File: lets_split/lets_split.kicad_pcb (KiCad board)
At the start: 2 copper layers, 112 x 79 mm, 62 parts, among them J1 3PIN, J2 6PIN, J3 3PIN, SW1 SW_PUSH, SW10 SW_PUSH, SW11 SW_PUSH, SW12 SW_PUSH, SW13 SW_PUSH, SW14 SW_PUSH, SW15 SW_PUSH, SW16 SW_PUSH, SW17 SW_PUSH, SW18 SW_PUSH, SW19 SW_PUSH, SW2 SW_PUSH, SW21 SW_PUSH, SW22 SW_PUSH, SW23 SW_PUSH, SW3 SW_PUSH, SW4 SW_PUSH, SW5 SW_PUSH, SW6 SW_PUSH, SW7 SW_PUSH, SW8 SW_PUSH, SW9 SW_PUSH, U2 HOLE, U3 HOLE, U4 HOLE, U5 HOLE

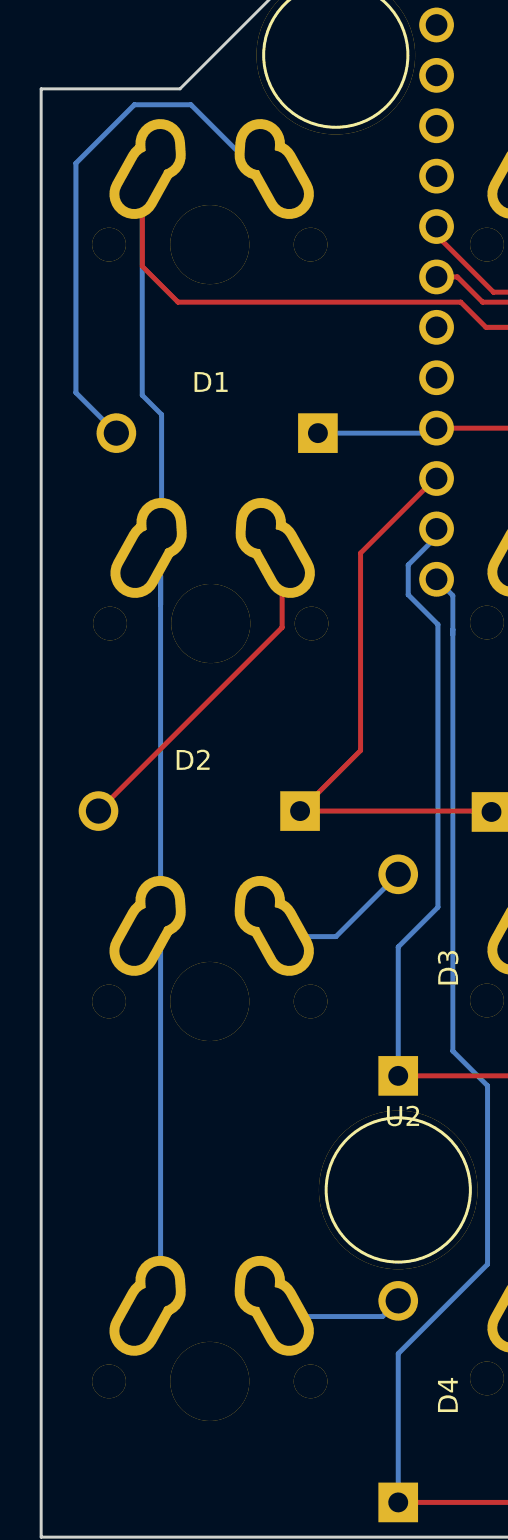
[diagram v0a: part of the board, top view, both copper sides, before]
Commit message: Fix alignments at left column
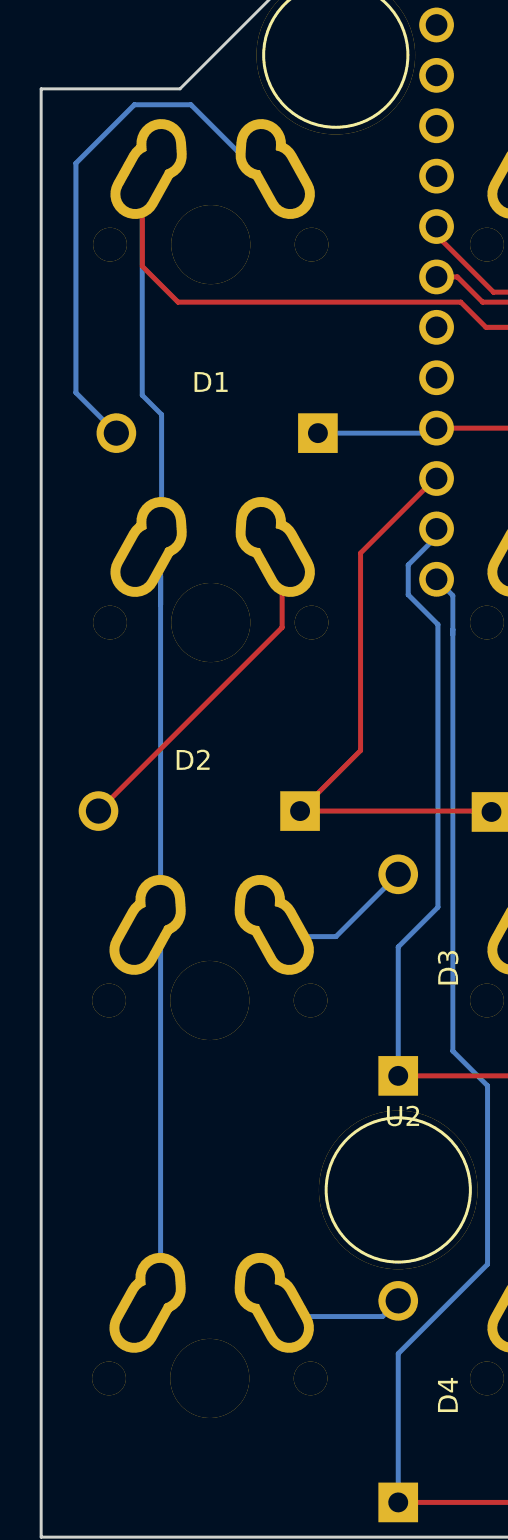
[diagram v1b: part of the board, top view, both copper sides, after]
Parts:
- moved SW4 0.15 mm to (45.5, 104.0)
